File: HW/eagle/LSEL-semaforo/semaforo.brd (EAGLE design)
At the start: 51 x 30 mm, 14 parts, among them J1 RJ11-2L-B, J3 RJ11-2L-B, U1 Tiny45-20-SMT

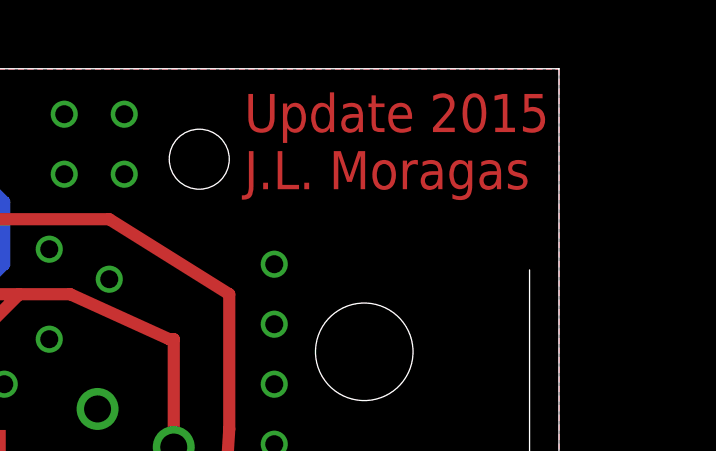
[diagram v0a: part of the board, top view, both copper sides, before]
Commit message: Barrera RJ changed
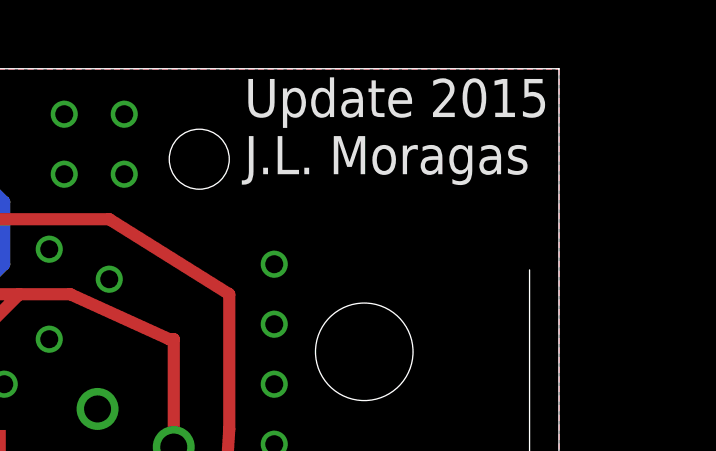
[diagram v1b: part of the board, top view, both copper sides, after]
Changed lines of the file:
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@@
 <text x="8.5" y="61" size="1.778" layer="1" font="vector" rot="R270" align="center">J. Gonzalez
 LSEL 2014</text>
-<text x="46.5" y="72.5" size="1.27" layer="1">Update 2015
+<text x="46.5" y="73" size="1.27" layer="21">Update 2015
 J.L. Moragas</text>
 </plain>

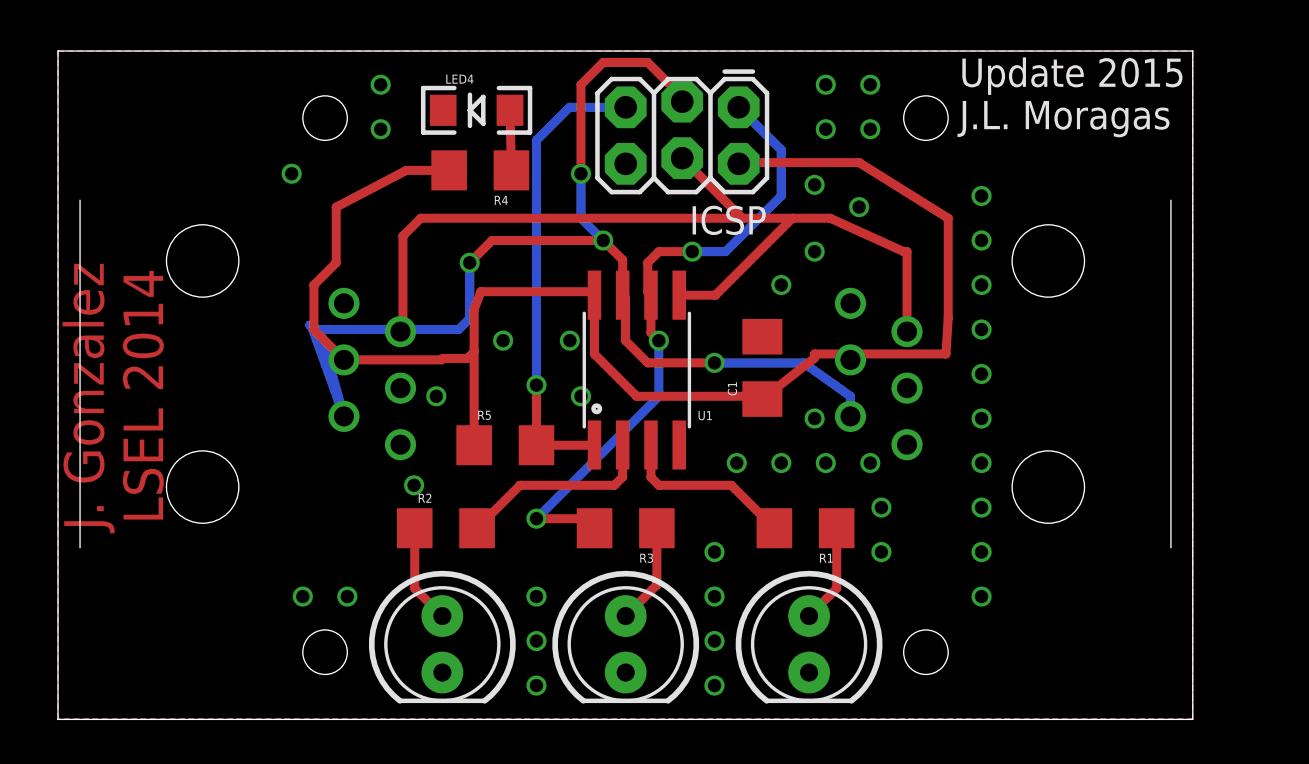
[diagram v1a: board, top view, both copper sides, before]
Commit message: Semaforo RJ changed
correction of mistakes
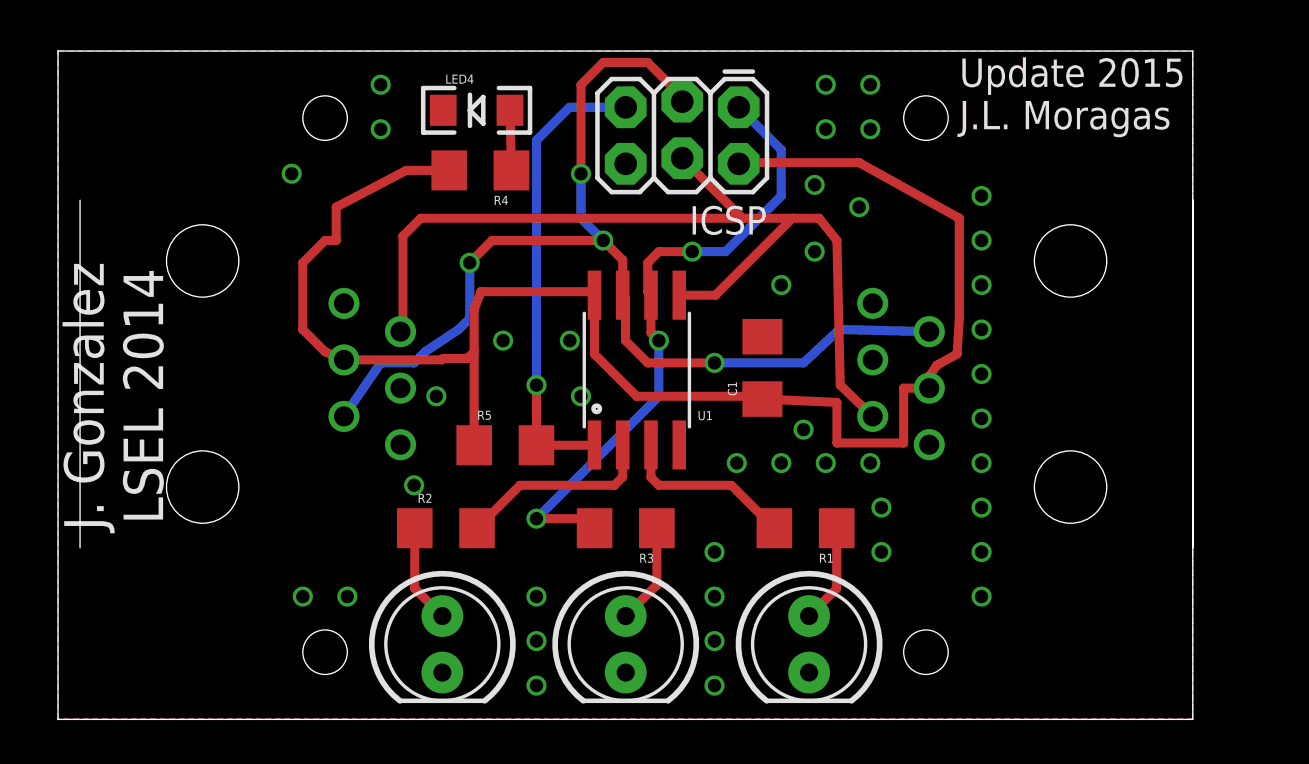
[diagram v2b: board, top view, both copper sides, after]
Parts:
- moved J1 1.00 mm to (51.5, 62.0)
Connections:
- net GND: now also J1.3; no longer J1.4
- net MOSI: now also J1.5; no longer J1.2
- net SCK: now also J1.2; no longer J1.5
- net VCC: now also J1.4; no longer J1.3
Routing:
- net VCC: track 68.1 -> 74.0 mm
- net SCK: track 55.0 -> 49.3 mm
- net MOSI: track 41.6 -> 43.5 mm
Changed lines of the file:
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@@
 <hole x="45" y="49.5" drill="2"/>
 <hole x="18" y="49.5" drill="2"/>
-<text x="8.5" y="61" size="1.778" layer="1" font="vector" rot="R270" align="center">J. Gonzalez
+<text x="8.5" y="61" size="1.778" layer="21" font="vector" rot="R270" align="center">J. Gonzalez
 LSEL 2014</text>
 <text x="46.5" y="73" size="1.27" layer="21">Update 2015
@@
 <attribute name="OC_FARNELL" value="unknown" x="12.5" y="62" size="1.778" layer="28" rot="MR90" display="off"/>
 </element>
-<element name="J1" library="con-tycoelectronics" package="RJ11-NO_SHIELD" value="RJ11-2L-B" x="50.5" y="62" rot="MR270">
-<attribute name="OC_NEWARK" value="83F4463" x="50.5" y="62" size="1.778" layer="28" rot="MR270" display="off"/>
-<attribute name="MPN" value="RJ11-2L-B" x="50.5" y="62" size="1.778" layer="28" rot="MR270" display="off"/>
-<attribute name="MF" value="TYCO ELECTRONICS" x="50.5" y="62" size="1.778" layer="28" rot="MR270" display="off"/>
-<attribute name="OC_FARNELL" value="unknown" x="50.5" y="62" size="1.778" layer="28" rot="MR270" display="off"/>
+<element name="J1" library="con-tycoelectronics" package="RJ11-NO_SHIELD" value="RJ11-2L-B" x="51.5" y="62" rot="MR270">
+<attribute name="OC_NEWARK" value="83F4463" x="51.5" y="62" size="1.778" layer="28" rot="MR270" display="off"/>
+<attribute name="MPN" value="RJ11-2L-B" x="51.5" y="62" size="1.778" layer="28" rot="MR270" display="off"/>
+<attribute name="MF" value="TYCO ELECTRONICS" x="51.5" y="62" size="1.778" layer="28" rot="MR270" display="off"/>
+<attribute name="OC_FARNELL" value="unknown" x="51.5" y="62" size="1.778" layer="28" rot="MR270" display="off"/>
 </element>
 </elements>
@@
 <contactref element="ICSP" pad="2"/>
 <contactref element="R5" pad="1"/>
-<wire x1="41.61" y1="62.9" x2="45.9" y2="62.9" width="0.4064" layer="1"/>
-<wire x1="45.9" y1="62.9" x2="46" y2="64.5" width="0.4064" layer="1"/>
-<wire x1="46" y1="64.5" x2="46" y2="69" width="0.4064" layer="1"/>
-<wire x1="46" y1="69" x2="42" y2="71.5" width="0.4064" layer="1"/>
+<wire x1="45.5" y1="62.4" x2="46.4" y2="62.9" width="0.4064" layer="1"/>
+<wire x1="46.4" y1="62.9" x2="46.5" y2="64.5" width="0.4064" layer="1"/>
+<wire x1="46.5" y1="64.5" x2="46.5" y2="69" width="0.4064" layer="1"/>
+<wire x1="46.5" y1="69" x2="42" y2="71.5" width="0.4064" layer="1"/>
 <wire x1="42" y1="71.5" x2="36.645" y2="71.5" width="0.4064" layer="1"/>
 <wire x1="36.645" y1="71.5" x2="36.59" y2="71.445" width="0.4064" layer="1"/>
@@
 <wire x1="30.105" y1="65.5428" x2="30.105" y2="62.895" width="0.4064" layer="1"/>
 <wire x1="30.105" y1="62.895" x2="32" y2="61" width="0.4064" layer="1"/>
-<wire x1="40" y1="62.725" x2="37.65" y2="60.875" width="0.4064" layer="1"/>
+<wire x1="41" y1="60.725" x2="37.65" y2="60.875" width="0.4064" layer="1"/>
 <wire x1="32" y1="61" x2="37.525" y2="61" width="0.4064" layer="1"/>
 <wire x1="37.525" y1="61" x2="37.65" y2="60.875" width="0.4064" layer="1"/>
@@
 <wire x1="25" y1="65.7" x2="29.9478" y2="65.7" width="0.4064" layer="1"/>
 <wire x1="29.9478" y1="65.7" x2="30.105" y2="65.5428" width="0.4064" layer="1"/>
-<wire x1="18.5" y1="69.5" x2="18.5" y2="67" width="0.4064" layer="1"/>
-<wire x1="18.5" y1="67" x2="17.5" y2="66" width="0.4064" layer="1"/>
-<wire x1="17.5" y1="66" x2="17.5" y2="63.985" width="0.4064" layer="1"/>
-<wire x1="17.8808125" y1="63.62931875" x2="17.8808125" y2="63.6041875" width="0.4064" layer="1"/>
-<wire x1="17.8808125" y1="63.6041875" x2="18.85" y2="62.635" width="0.4064" layer="1"/>
+<wire x1="18.5" y1="69.5" x2="18.5" y2="68" width="0.4064" layer="1"/>
 <wire x1="18.85" y1="62.635" x2="23.235" y2="62.635" width="0.4064" layer="1"/>
 <wire x1="23.3" y1="62.7" x2="24.4" y2="62.7" width="0.4064" layer="1"/>
 <wire x1="24.4" y1="62.7" x2="24.7" y2="63" width="0.4064" layer="1"/>
-<wire x1="17.5" y1="63.985" x2="17.8808125" y2="63.6041875" width="0.4064" layer="1"/>
 <wire x1="23.235" y1="62.635" x2="23.3" y2="62.7" width="0.4064" layer="1"/>
 <wire x1="24.7" y1="63" x2="24.7" y2="64.9" width="0.4064" layer="1"/>
 <wire x1="24.7" y1="64.9" x2="25" y2="65.7" width="0.4064" layer="1"/>
-<contactref element="J1" pad="3"/>
-<wire x1="41.61" y1="62.9" x2="41.61" y2="62.635" width="0.4064" layer="1"/>
-<wire x1="41.61" y1="62.9" x2="40" y2="62.9" width="0.4064" layer="1"/>
-<wire x1="40" y1="62.9" x2="40" y2="62.725" width="0.4064" layer="1"/>
+<contactref element="J1" pad="4"/>
+<wire x1="44" y1="61.365" x2="45.15" y2="61.365" width="0.4064" layer="1"/>
+<wire x1="44" y1="58.9" x2="41" y2="58.9" width="0.4064" layer="1"/>
+<wire x1="41" y1="58.9" x2="41" y2="60.725" width="0.4064" layer="1"/>
+<wire x1="44" y1="58.9" x2="44" y2="61.365" width="0.4064" layer="1"/>
+<wire x1="45.5" y1="62.4" x2="45.15" y2="61.9" width="0.4064" layer="1"/>
+<wire x1="45.15" y1="61.9" x2="45.15" y2="61.365" width="0.4064" layer="1"/>
+<wire x1="18.5" y1="68" x2="18" y2="68" width="0.4064" layer="1"/>
+<wire x1="18" y1="68" x2="17" y2="67" width="0.4064" layer="1"/>
+<wire x1="17" y1="67" x2="17" y2="64" width="0.4064" layer="1"/>
+<wire x1="17" y1="64" x2="18" y2="63" width="0.4064" layer="1"/>
+<wire x1="18" y1="63" x2="18.85" y2="62.635" width="0.4064" layer="1"/>
 </signal>
 <signal name="N$5">
@@
 <via x="38.5" y="58" extent="1-16" drill="0.6" diameter="0.6096"/>
 <via x="36.5" y="58" extent="1-16" drill="0.6" diameter="0.6096"/>
-<via x="40" y="60" extent="1-16" drill="0.6" diameter="0.6096"/>
+<via x="39.5" y="59.5" extent="1-16" drill="0.6" diameter="0.6096"/>
 <via x="35.5" y="50" extent="1-16" drill="0.6" diameter="0.6096"/>
 <via x="35.5" y="48" extent="1-16" drill="0.6" diameter="0.6096"/>
@@
 <via x="20.5" y="73" extent="1-16" drill="0.6" diameter="0.6096"/>
 <contactref element="J3" pad="3"/>
-<contactref element="J1" pad="4"/>
+<contactref element="J1" pad="3"/>
 </signal>
 <signal name="N$8">
@@
 <wire x1="31.5" y1="65.4178" x2="31.375" y2="65.5428" width="0.4064" layer="1"/>
 <contactref element="J3" pad="2"/>
-<wire x1="17.3" y1="64.2" x2="17.5" y2="64" width="0.4064" layer="16"/>
-<wire x1="17.5" y1="64" x2="17.755" y2="64" width="0.4064" layer="16"/>
-<wire x1="17.755" y1="64" x2="18.85" y2="60.095" width="0.4064" layer="16"/>
 <wire x1="24.5" y1="64.5" x2="24" y2="64" width="0.4064" layer="16"/>
-<wire x1="24" y1="64" x2="17.445" y2="64" width="0.4064" layer="16"/>
-<wire x1="17.445" y1="64" x2="18.85" y2="60.095" width="0.4064" layer="16"/>
-<contactref element="J1" pad="5"/>
-<wire x1="39.5" y1="62.5" x2="41.61" y2="61" width="0.4064" layer="16"/>
-<wire x1="41.61" y1="61" x2="41.61" y2="60.095" width="0.4064" layer="16"/>
+<contactref element="J1" pad="2"/>
+<wire x1="39.5" y1="62.5" x2="41.11" y2="64" width="0.4064" layer="16"/>
+<wire x1="41.11" y1="64" x2="45.15" y2="63.905" width="0.4064" layer="16"/>
+<wire x1="24" y1="64" x2="22.5" y2="63" width="0.4064" layer="16"/>
+<wire x1="22.5" y1="63" x2="22" y2="62.5" width="0.4064" layer="16"/>
+<wire x1="22" y1="62.5" x2="20.5" y2="62.5" width="0.4064" layer="16"/>
+<wire x1="20.5" y1="62.5" x2="18.85" y2="60.095" width="0.4064" layer="16"/>
 </signal>
 <signal name="MOSI">
 <contactref element="ICSP" pad="4"/>
-<wire x1="44" y1="67.5" x2="40.7" y2="69" width="0.4064" layer="1"/>
+<wire x1="41" y1="68" x2="40.2" y2="69" width="0.4064" layer="1"/>
 <wire x1="36.749" y1="69" x2="22.3" y2="69" width="0.4064" layer="1"/>
-<wire x1="40.7" y1="69" x2="39" y2="69" width="0.4064" layer="1"/>
+<wire x1="40.2" y1="69" x2="39" y2="69" width="0.4064" layer="1"/>
 <wire x1="39" y1="69" x2="36.749" y2="69" width="0.4064" layer="1"/>
 <wire x1="36.749" y1="69" x2="34.05" y2="71.699" width="0.4064" layer="1"/>
@@
 <wire x1="21.5" y1="68.2" x2="21.5" y2="64.015" width="0.4064" layer="1"/>
 <wire x1="21.5" y1="64.015" x2="21.39" y2="63.905" width="0.4064" layer="1"/>
-<contactref element="J1" pad="2"/>
-<wire x1="44" y1="67.5" x2="44.15" y2="67.5" width="0.4064" layer="1"/>
-<wire x1="44.15" y1="67.5" x2="44.15" y2="63.905" width="0.4064" layer="1"/>
+<contactref element="J1" pad="5"/>
+<wire x1="41" y1="68" x2="41.15" y2="61.5" width="0.4064" layer="1"/>
+<wire x1="41.15" y1="61.5" x2="42.61" y2="60.095" width="0.4064" layer="1"/>
 </signal>
 </signals>
